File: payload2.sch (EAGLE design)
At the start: 26 parts, among them U1 ATMEGA328P_TQFP, U2 USD-SOCKETSMD, U3 3.3V/150mA, U4 9DoF IMU, Y1 16MHz

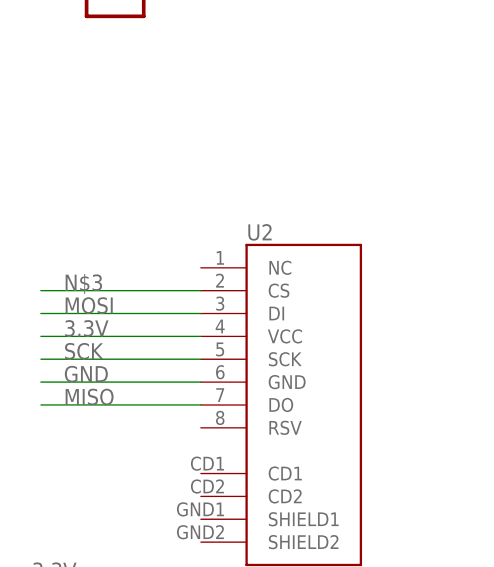
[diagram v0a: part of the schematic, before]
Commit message: added connection to sd card
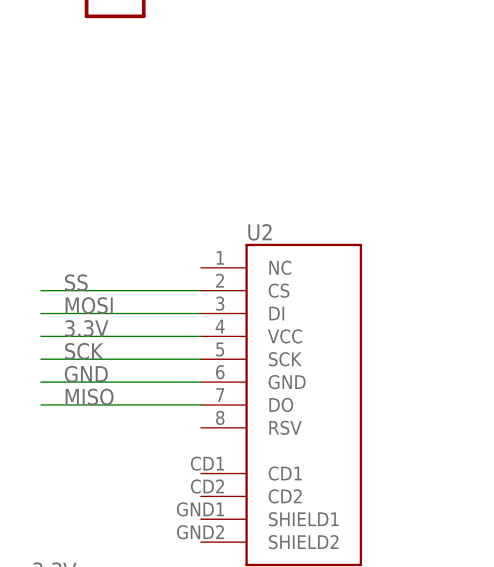
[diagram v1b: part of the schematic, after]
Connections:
- removed net N$3: U2.CS
- net SS: now also U2.CS
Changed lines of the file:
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@@
 <label x="-48.26" y="124.46" size="1.778" layer="95"/>
+</segment>
+<segment>
+<pinref part="U2" gate="G$1" pin="CS"/>
+<wire x1="-243.84" y1="76.2" x2="-261.62" y2="76.2" width="0.1524" layer="91"/>
+<label x="-259.08" y="76.2" size="1.778" layer="95"/>
 </segment>
 </net>
@@
 </segment>
 </net>
-<net name="N$3" class="0">
-<segment>
-<pinref part="U2" gate="G$1" pin="CS"/>
-<wire x1="-243.84" y1="76.2" x2="-261.62" y2="76.2" width="0.1524" layer="91"/>
-<label x="-259.08" y="76.2" size="1.778" layer="95"/>
-</segment>
-</net>

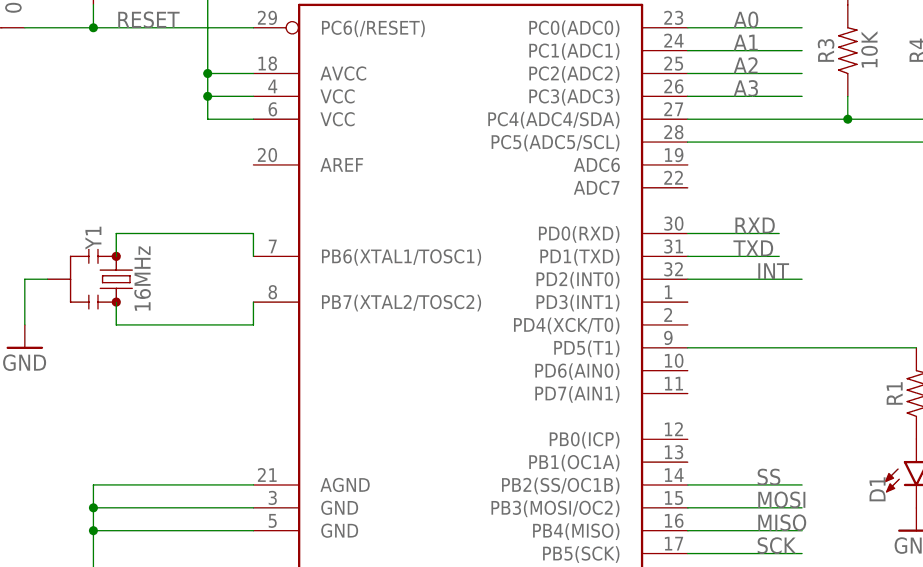
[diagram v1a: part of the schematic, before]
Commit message: Started moving components in board file
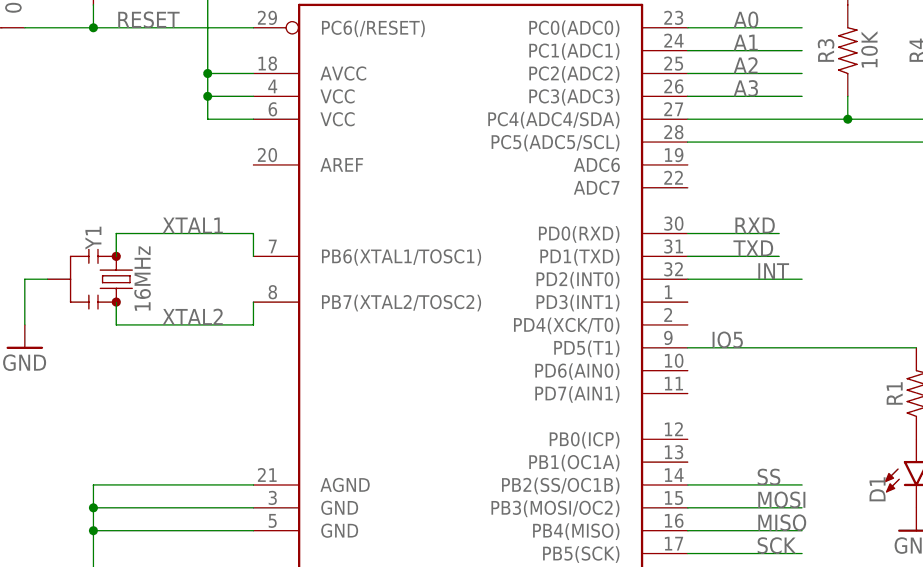
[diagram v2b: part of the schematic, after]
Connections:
- net N$11 renamed XTAL2
- net N$8 renamed IO5
- net N$9 renamed XTAL1
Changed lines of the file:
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@@
 </segment>
 </net>
-<net name="N$8" class="0">
+<net name="IO5" class="0">
 <segment>
 <pinref part="U1" gate="U$1" pin="PD5(T1)"/>
 <pinref part="R1" gate="G$1" pin="2"/>
 <wire x1="-55.88" y1="139.7" x2="-30.48" y2="139.7" width="0.1524" layer="91"/>
+<label x="-53.34" y="139.7" size="1.778" layer="95"/>
 </segment>
 </net>
@@
 </segment>
 </net>
-<net name="N$9" class="0">
+<net name="XTAL1" class="0">
 <segment>
 <pinref part="Y1" gate="G$1" pin="1"/>
@@
 <pinref part="U1" gate="U$1" pin="PB6(XTAL1/TOSC1)"/>
 <wire x1="-104.14" y1="149.86" x2="-104.14" y2="152.4" width="0.1524" layer="91"/>
+<label x="-114.3" y="152.4" size="1.778" layer="95"/>
 </segment>
 </net>
-<net name="N$11" class="0">
+<net name="XTAL2" class="0">
 <segment>
 <pinref part="Y1" gate="G$1" pin="3"/>
@@
 <pinref part="U1" gate="U$1" pin="PB7(XTAL2/TOSC2)"/>
 <wire x1="-104.14" y1="144.78" x2="-104.14" y2="142.24" width="0.1524" layer="91"/>
+<label x="-114.3" y="142.24" size="1.778" layer="95"/>
 </segment>
 </net>

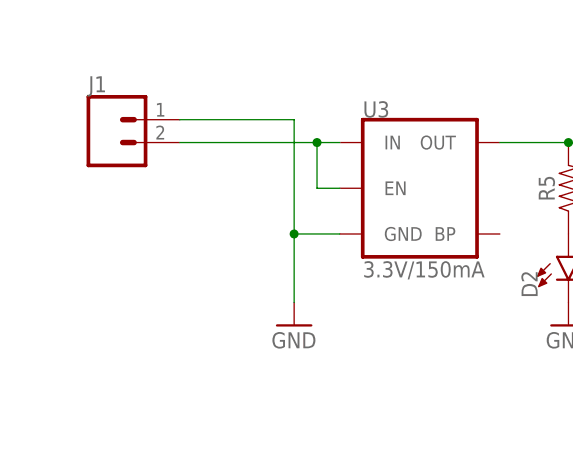
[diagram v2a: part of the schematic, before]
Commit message: Worked on routing on board file.  Added screw switch connectors.
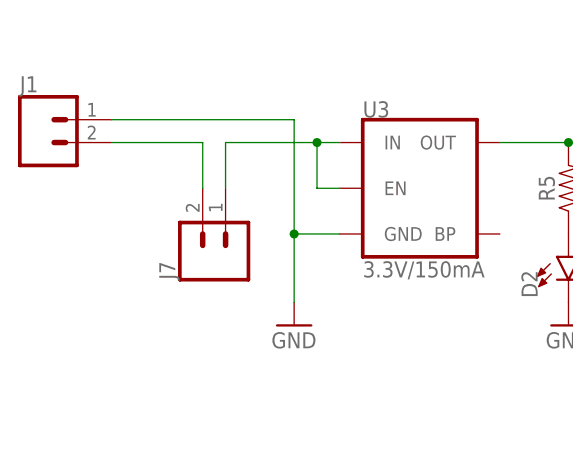
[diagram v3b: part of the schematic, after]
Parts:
- added J7: (no value), SparkFun-Connectors:CONN_02
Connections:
- new net N$1: J1.1, J7.2
- net N$4: now also J7.1; no longer J1.1
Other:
- moved on the sheet: J1
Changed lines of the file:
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@@
 <part name="GND13" library="femtosat" deviceset="GND" device=""/>
 <part name="P+10" library="femtosat" deviceset="3.3V" device=""/>
+<part name="J7" library="SparkFun-Connectors" deviceset="CONN_02" device=""/>
 </parts>
 <sheets>
@@
 <instance part="P+6" gate="G$1" x="-261.62" y="40.64"/>
 <instance part="GND6" gate="1" x="-261.62" y="5.08"/>
-<instance part="J1" gate="G$1" x="-256.54" y="182.88"/>
+<instance part="J1" gate="G$1" x="-264.16" y="182.88"/>
 <instance part="GND7" gate="1" x="-208.28" y="12.7"/>
 <instance part="C2" gate="G$1" x="-256.54" y="12.7"/>
@@
 <instance part="GND13" gate="1" x="-111.76" y="50.8"/>
 <instance part="P+10" gate="G$1" x="-111.76" y="83.82"/>
+<instance part="J7" gate="G$1" x="-243.84" y="170.18" rot="R90"/>
 </instances>
 <busses>
@@
 <wire x1="-236.22" y1="172.72" x2="-231.14" y2="172.72" width="0.1524" layer="91"/>
 <pinref part="J1" gate="G$1" pin="2"/>
-<wire x1="-248.92" y1="185.42" x2="-236.22" y2="185.42" width="0.1524" layer="91"/>
+<wire x1="-256.54" y1="185.42" x2="-236.22" y2="185.42" width="0.1524" layer="91"/>
 <wire x1="-236.22" y1="185.42" x2="-236.22" y2="172.72" width="0.1524" layer="91"/>
 <junction x="-236.22" y="172.72"/>
@@
 <net name="N$4" class="0">
 <segment>
-<pinref part="J1" gate="G$1" pin="1"/>
 <pinref part="U3" gate="U1" pin="IN"/>
-<wire x1="-248.92" y1="182.88" x2="-233.68" y2="182.88" width="0.1524" layer="91"/>
 <pinref part="U3" gate="U1" pin="EN"/>
 <wire x1="-233.68" y1="182.88" x2="-231.14" y2="182.88" width="0.1524" layer="91"/>
 <wire x1="-231.14" y1="177.8" x2="-233.68" y2="177.8" width="0.1524" layer="91"/>
 <wire x1="-233.68" y1="177.8" x2="-233.68" y2="182.88" width="0.1524" layer="91"/>
+<pinref part="J7" gate="G$1" pin="1"/>
+<wire x1="-243.84" y1="177.8" x2="-243.84" y2="182.88" width="0.1524" layer="91"/>
+<wire x1="-243.84" y1="182.88" x2="-233.68" y2="182.88" width="0.1524" layer="91"/>
 <junction x="-233.68" y="182.88"/>
 </segment>
@@
 </segment>
 </net>
+<net name="N$1" class="0">
+<segment>
+<pinref part="J1" gate="G$1" pin="1"/>
+<pinref part="J7" gate="G$1" pin="2"/>
+<wire x1="-256.54" y1="182.88" x2="-246.38" y2="182.88" width="0.1524" layer="91"/>
+<wire x1="-246.38" y1="182.88" x2="-246.38" y2="177.8" width="0.1524" layer="91"/>
+</segment>
+</net>

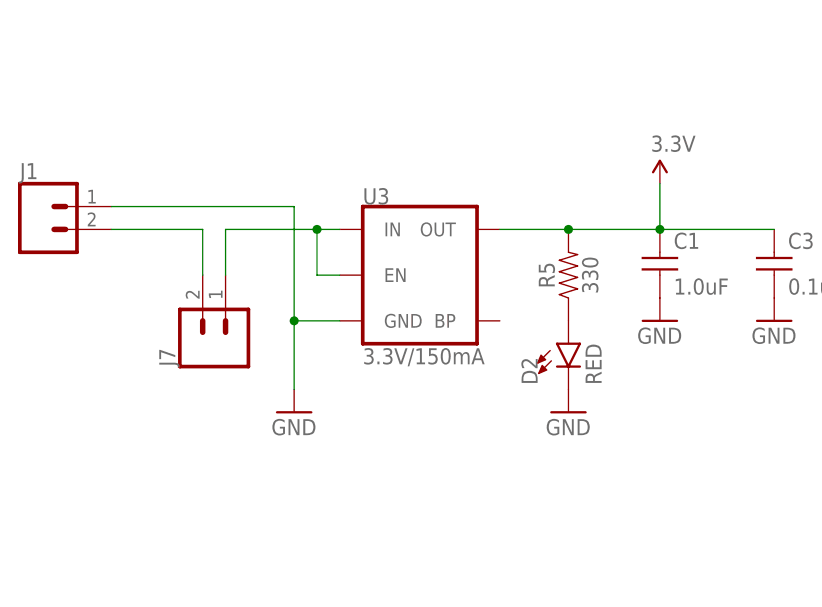
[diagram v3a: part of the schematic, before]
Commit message: Finalized board design.  Worked screw sizes and possitioning.  Switched two hole connector for battery connector.  added jumpers for battery charger.
Board should be ready to order.  Things that still need to improve:
1) final check and look over.
2) silk screen could be improved.
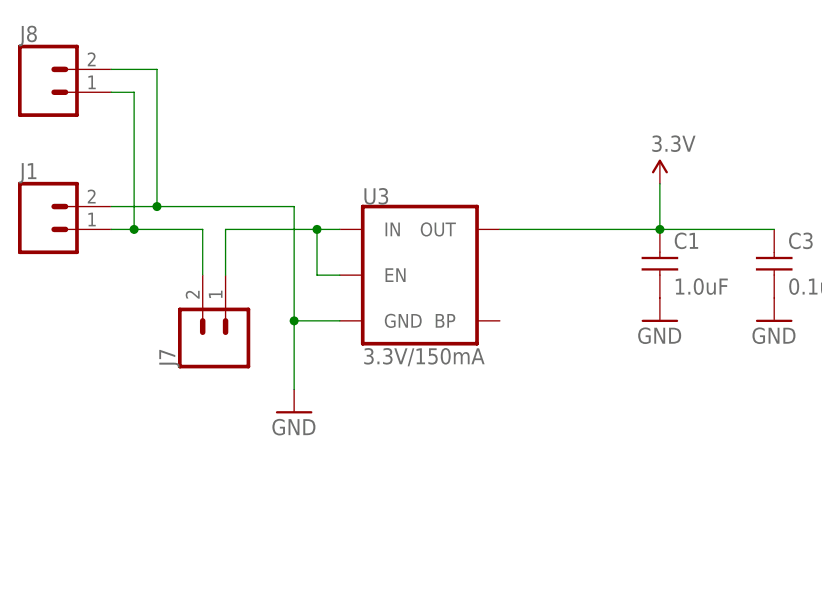
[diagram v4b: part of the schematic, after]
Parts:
- removed D2: RED, femtosat:LED_RED0603
- removed R5: 330, femtosat:RESISTOR_330OHM-0603-1/10W-1%
- added J8: (no value), SparkFun-Connectors:CONN_02
- J1: device femtosat:CONNECTOR_2PIN-JST-2MM-SMT -> SparkFun-Connectors:CONN_02
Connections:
- removed net N$1: J1.1, J7.2
- removed net N$10: D2.A, R5.1
- new net VIN: J1.1, J7.2, J8.1
- net 3.3V: no longer R5.2
- net GND: now also J8.2; no longer D2.C
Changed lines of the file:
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@@
 <part name="P+6" library="femtosat" deviceset="3.3V" device=""/>
 <part name="GND6" library="femtosat" deviceset="GND" device=""/>
-<part name="J1" library="femtosat" deviceset="CONNECTOR_2PIN" device="-JST-2MM-SMT"/>
+<part name="J1" library="SparkFun-Connectors" deviceset="CONN_02" device=""/>
 <part name="GND7" library="femtosat" deviceset="GND" device=""/>
 <part name="C2" library="femtosat" deviceset="CAPACITOR_0.1UF" device="" value="0.1uF"/>
@@
 <part name="C4" library="femtosat" deviceset="CAPACITOR_0.1UF" device="" value="0.1uF"/>
 <part name="J2" library="femtosat" deviceset="CONNECTOR_6PIN" device="SILK_FEMALE_PTH"/>
-<part name="D2" library="femtosat" deviceset="LED_RED" device="0603" value="RED"/>
-<part name="R5" library="femtosat" deviceset="RESISTOR_330OHM" device="-0603-1/10W-1%" value="330"/>
-<part name="GND11" library="femtosat" deviceset="GND" device=""/>
 <part name="U2" library="microSD-Breakout-v14" deviceset="USD-SOCKET" device="SMD"/>
 <part name="J3" library="SparkFun-Connectors" deviceset="CONN_02" device=""/>
@@
 <part name="P+10" library="femtosat" deviceset="3.3V" device=""/>
 <part name="J7" library="SparkFun-Connectors" deviceset="CONN_02" device=""/>
+<part name="J8" library="SparkFun-Connectors" deviceset="CONN_02" device=""/>
 </parts>
 <sheets>
@@
 <instance part="C4" gate="G$1" x="-132.08" y="175.26" rot="R90"/>
 <instance part="J2" gate="G$1" x="-251.46" y="114.3"/>
-<instance part="D2" gate="G$1" x="-205.74" y="170.18"/>
-<instance part="R5" gate="G$1" x="-205.74" y="177.8" rot="R90"/>
-<instance part="GND11" gate="1" x="-205.74" y="162.56"/>
 <instance part="U2" gate="G$1" x="-236.22" y="66.04"/>
 <instance part="J3" gate="G$1" x="-177.8" y="60.96"/>
@@
 <instance part="P+10" gate="G$1" x="-111.76" y="83.82"/>
 <instance part="J7" gate="G$1" x="-243.84" y="170.18" rot="R90"/>
+<instance part="J8" gate="G$1" x="-264.16" y="198.12"/>
 </instances>
 <busses>
@@
 <wire x1="-236.22" y1="172.72" x2="-231.14" y2="172.72" width="0.1524" layer="91"/>
 <pinref part="J1" gate="G$1" pin="2"/>
-<wire x1="-256.54" y1="185.42" x2="-236.22" y2="185.42" width="0.1524" layer="91"/>
+<wire x1="-256.54" y1="185.42" x2="-251.46" y2="185.42" width="0.1524" layer="91"/>
+<wire x1="-251.46" y1="185.42" x2="-236.22" y2="185.42" width="0.1524" layer="91"/>
 <wire x1="-236.22" y1="185.42" x2="-236.22" y2="172.72" width="0.1524" layer="91"/>
 <junction x="-236.22" y="172.72"/>
+<pinref part="J8" gate="G$1" pin="2"/>
+<wire x1="-256.54" y1="200.66" x2="-251.46" y2="200.66" width="0.1524" layer="91"/>
+<wire x1="-251.46" y1="200.66" x2="-251.46" y2="185.42" width="0.1524" layer="91"/>
+<junction x="-251.46" y="185.42"/>
 </segment>
 <segment>
@@
 <wire x1="-246.38" y1="119.38" x2="-238.76" y2="119.38" width="0.1524" layer="91"/>
 <label x="-243.84" y="119.38" size="1.778" layer="95"/>
-</segment>
-<segment>
-<pinref part="D2" gate="G$1" pin="C"/>
-<pinref part="GND11" gate="1" pin="GND"/>
 </segment>
 <segment>
@@
 <pinref part="U3" gate="U1" pin="OUT"/>
 <pinref part="C1" gate="G$1" pin="1"/>
-<wire x1="-213.36" y1="182.88" x2="-205.74" y2="182.88" width="0.1524" layer="91"/>
 <pinref part="P+2" gate="G$1" pin="3.3V"/>
-<wire x1="-205.74" y1="182.88" x2="-195.58" y2="182.88" width="0.1524" layer="91"/>
+<wire x1="-213.36" y1="182.88" x2="-195.58" y2="182.88" width="0.1524" layer="91"/>
 <wire x1="-195.58" y1="182.88" x2="-195.58" y2="187.96" width="0.1524" layer="91"/>
 <junction x="-195.58" y="182.88"/>
 <pinref part="C3" gate="G$1" pin="1"/>
 <wire x1="-195.58" y1="182.88" x2="-182.88" y2="182.88" width="0.1524" layer="91"/>
-<pinref part="R5" gate="G$1" pin="2"/>
-<junction x="-205.74" y="182.88"/>
 </segment>
 <segment>
@@
 </segment>
 </net>
-<net name="N$10" class="0">
-<segment>
-<pinref part="D2" gate="G$1" pin="A"/>
-<pinref part="R5" gate="G$1" pin="1"/>
-</segment>
-</net>
 <net name="XTAL1" class="0">
 <segment>
@@
 </segment>
 </net>
-<net name="N$1" class="0">
+<net name="VIN" class="0">
 <segment>
 <pinref part="J1" gate="G$1" pin="1"/>
 <pinref part="J7" gate="G$1" pin="2"/>
-<wire x1="-256.54" y1="182.88" x2="-246.38" y2="182.88" width="0.1524" layer="91"/>
+<wire x1="-256.54" y1="182.88" x2="-254" y2="182.88" width="0.1524" layer="91"/>
+<wire x1="-254" y1="182.88" x2="-246.38" y2="182.88" width="0.1524" layer="91"/>
 <wire x1="-246.38" y1="182.88" x2="-246.38" y2="177.8" width="0.1524" layer="91"/>
-</segment>
-</net>
+<pinref part="J8" gate="G$1" pin="1"/>
+<wire x1="-256.54" y1="198.12" x2="-254" y2="198.12" width="0.1524" layer="91"/>
+<wire x1="-254" y1="198.12" x2="-254" y2="182.88" width="0.1524" layer="91"/>
+<junction x="-254" y="182.88"/>
+</segment>
+</net>

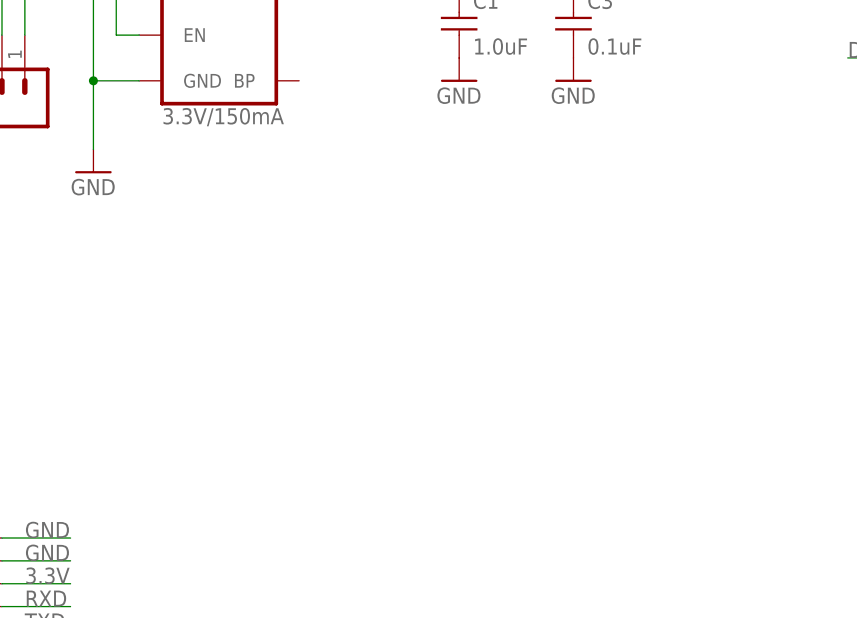
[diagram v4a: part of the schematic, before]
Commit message: Added pressure sensor for gits and giggles.
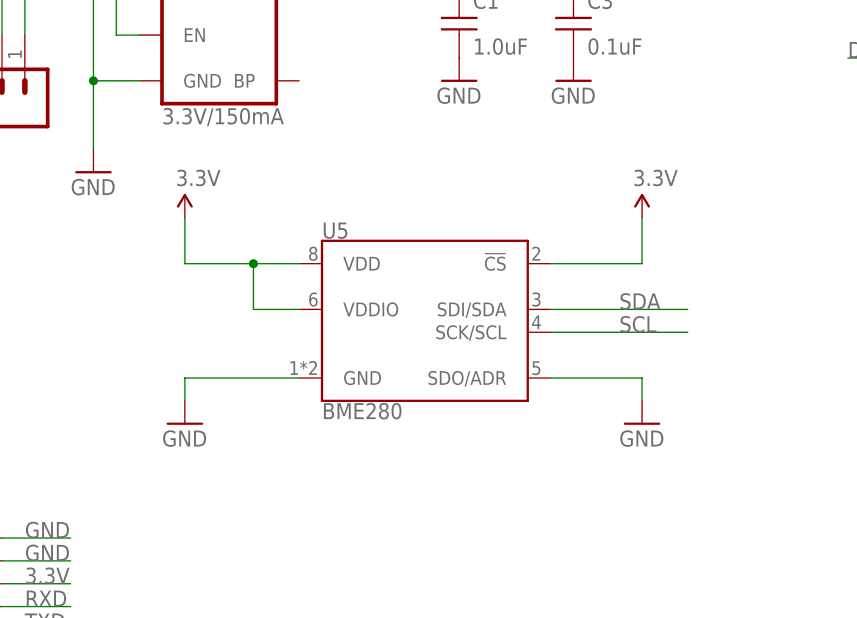
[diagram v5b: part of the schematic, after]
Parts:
- added U5: BME280, femtosat:BME280
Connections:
- net 3.3V: now also U5.!CS, U5.VDD, U5.VDDIO
- net GND: now also U5.GND, U5.SDO/ADR
- net SCL: now also U5.SCK/SCL
- net SDA: now also U5.SDI/SDA
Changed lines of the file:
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@@
 <part name="J7" library="SparkFun-Connectors" deviceset="CONN_02" device=""/>
 <part name="J8" library="SparkFun-Connectors" deviceset="CONN_02" device=""/>
+<part name="U5" library="femtosat" deviceset="BME280" device="" value="BME280"/>
+<part name="P+11" library="femtosat" deviceset="3.3V" device=""/>
+<part name="GND11" library="femtosat" deviceset="GND" device=""/>
+<part name="P+12" library="femtosat" deviceset="3.3V" device=""/>
+<part name="GND14" library="femtosat" deviceset="GND" device=""/>
 </parts>
 <sheets>
@@
 <instance part="J7" gate="G$1" x="-243.84" y="170.18" rot="R90"/>
 <instance part="J8" gate="G$1" x="-264.16" y="198.12"/>
+<instance part="U5" gate="U1" x="-200.66" y="147.32"/>
+<instance part="P+11" gate="G$1" x="-226.06" y="157.48"/>
+<instance part="GND11" gate="1" x="-226.06" y="134.62"/>
+<instance part="P+12" gate="G$1" x="-175.26" y="157.48"/>
+<instance part="GND14" gate="1" x="-175.26" y="134.62"/>
 </instances>
 <busses>
@@
 <pinref part="GND13" gate="1" pin="GND"/>
 </segment>
+<segment>
+<pinref part="U5" gate="U1" pin="GND"/>
+<wire x1="-213.36" y1="139.7" x2="-226.06" y2="139.7" width="0.1524" layer="91"/>
+<wire x1="-226.06" y1="139.7" x2="-226.06" y2="137.16" width="0.1524" layer="91"/>
+<pinref part="GND11" gate="1" pin="GND"/>
+</segment>
+<segment>
+<pinref part="U5" gate="U1" pin="SDO/ADR"/>
+<wire x1="-185.42" y1="139.7" x2="-175.26" y2="139.7" width="0.1524" layer="91"/>
+<wire x1="-175.26" y1="139.7" x2="-175.26" y2="137.16" width="0.1524" layer="91"/>
+<pinref part="GND14" gate="1" pin="GND"/>
+</segment>
 </net>
 <net name="3.3V" class="0">
@@
 <wire x1="-111.76" y1="83.82" x2="-111.76" y2="78.74" width="0.1524" layer="91"/>
 </segment>
+<segment>
+<pinref part="U5" gate="U1" pin="VDD"/>
+<wire x1="-213.36" y1="152.4" x2="-218.44" y2="152.4" width="0.1524" layer="91"/>
+<pinref part="U5" gate="U1" pin="VDDIO"/>
+<wire x1="-218.44" y1="152.4" x2="-226.06" y2="152.4" width="0.1524" layer="91"/>
+<wire x1="-213.36" y1="147.32" x2="-218.44" y2="147.32" width="0.1524" layer="91"/>
+<wire x1="-218.44" y1="147.32" x2="-218.44" y2="152.4" width="0.1524" layer="91"/>
+<junction x="-218.44" y="152.4"/>
+<pinref part="P+11" gate="G$1" pin="3.3V"/>
+<wire x1="-226.06" y1="157.48" x2="-226.06" y2="152.4" width="0.1524" layer="91"/>
+</segment>
+<segment>
+<pinref part="U5" gate="U1" pin="!CS"/>
+<wire x1="-185.42" y1="152.4" x2="-175.26" y2="152.4" width="0.1524" layer="91"/>
+<wire x1="-175.26" y1="152.4" x2="-175.26" y2="157.48" width="0.1524" layer="91"/>
+<pinref part="P+12" gate="G$1" pin="3.3V"/>
+</segment>
 </net>
 <net name="MISO" class="0">
@@
 <label x="-213.36" y="22.86" size="1.778" layer="95"/>
 </segment>
+<segment>
+<pinref part="U5" gate="U1" pin="SDI/SDA"/>
+<wire x1="-185.42" y1="147.32" x2="-170.18" y2="147.32" width="0.1524" layer="91"/>
+<label x="-177.8" y="147.32" size="1.778" layer="95"/>
+</segment>
 </net>
 <net name="SCL" class="0">
@@
 <label x="-213.36" y="25.4" size="1.778" layer="95"/>
 </segment>
-</net>
+<segment>
+<pinref part="U5" gate="U1" pin="SCK/SCL"/>
+<wire x1="-185.42" y1="144.78" x2="-170.18" y2="144.78" width="0.1524" layer="91"/>
+<label x="-177.8" y="144.78" size="1.778" layer="95"/>
+</segment>
+</net>
